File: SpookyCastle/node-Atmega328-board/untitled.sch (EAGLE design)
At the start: 24 parts, among them IC2 MEGA48/88/168-AU, J1 RJ11-6PTH

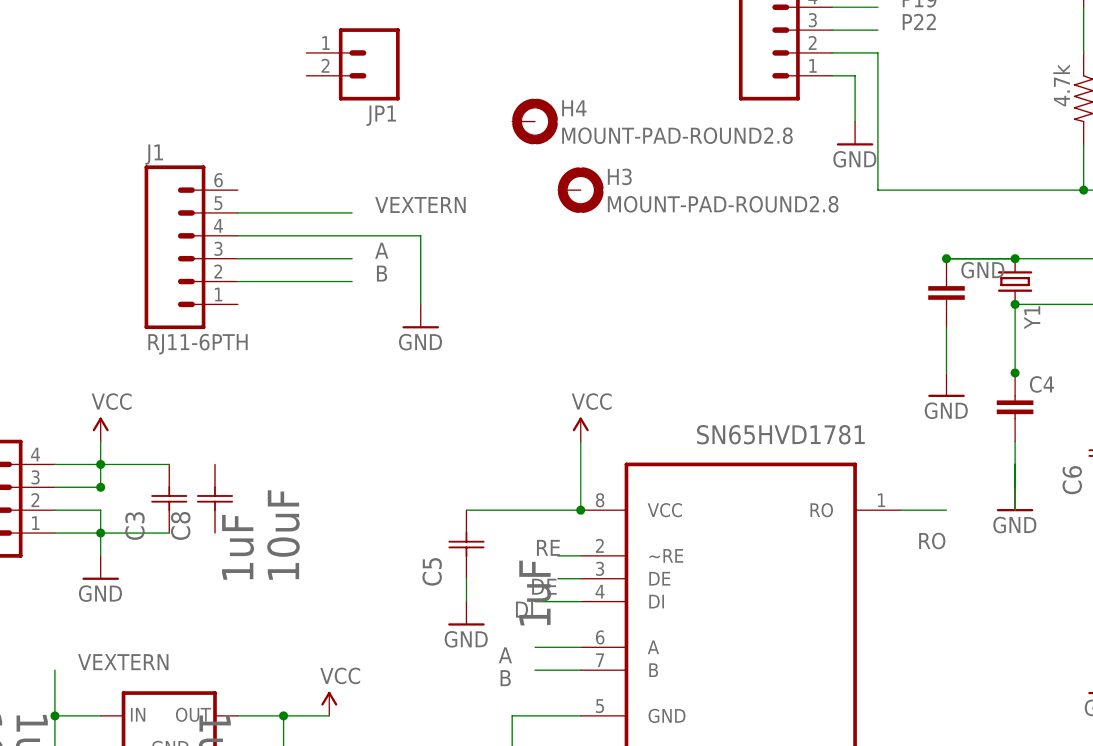
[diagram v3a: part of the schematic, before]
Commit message: Added a buncha silk to the board.
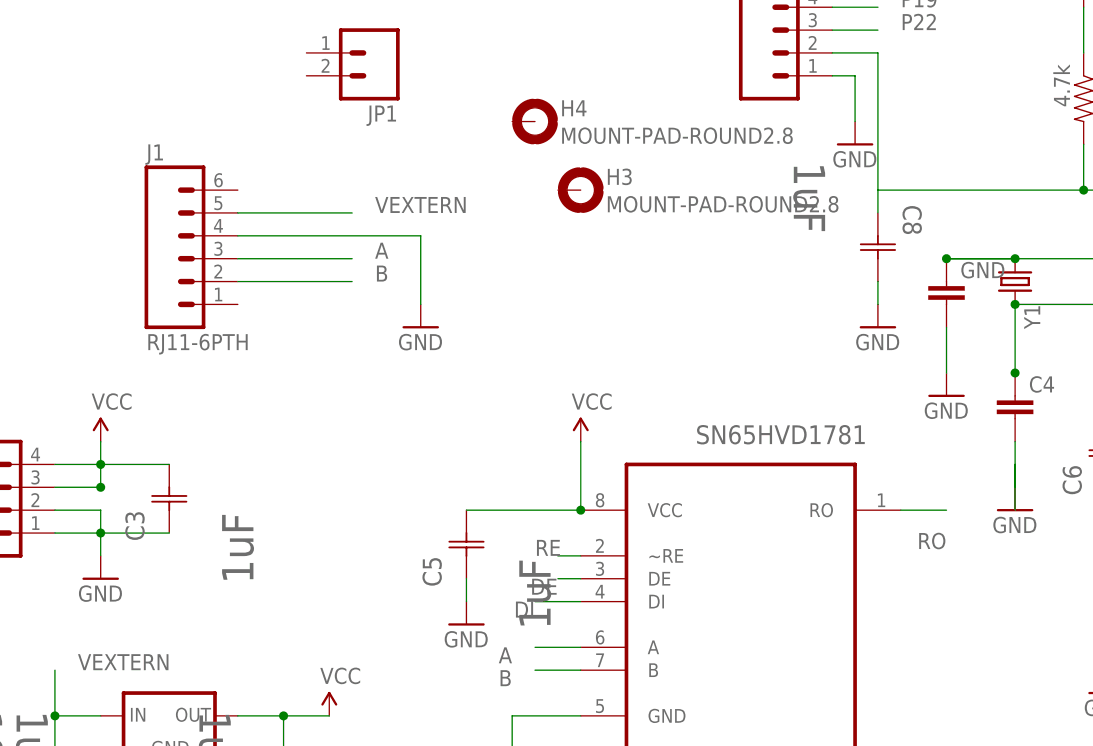
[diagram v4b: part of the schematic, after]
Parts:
- C8: value 10uF -> 1uF; device Murata_By_element14_Batch_1:GRM32ER7YA106KA12L -> Murata_By_element14_Batch_1:GRM21BR71H105KA12L; MPN GRM32ER7YA106KA12L -> GRM21BR71H105KA12L; OC_FARNELL 1735537 -> 1735541; OC_NEWARK 24R2634 -> 24R6342; VALUE 10uF -> 1uF; VOLTAGERATING 35V -> 50V
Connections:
- net GND: now also C8.C2
- net N$22: now also C8.C1
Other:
- moved on the sheet: C8
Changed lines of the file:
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@@
 <part name="R1" library="SparkFun - Copy" deviceset="RESISTOR" device="0805-RES" value="4.7k"/>
 <part name="P+5" library="SparkFun - Copy" deviceset="VCC" device=""/>
-<part name="C8" library="Murata_By_element14_Batch_1" deviceset="GRM32ER7YA106KA12L" device="" value="10uF">
-<attribute name="MPN" value="GRM32ER7YA106KA12L"/>
-<attribute name="OC_FARNELL" value="1735537"/>
-<attribute name="OC_NEWARK" value="24R2634"/>
+<part name="GND11" library="SparkFun - Copy" deviceset="GND" device=""/>
+<part name="C8" library="Murata_By_element14_Batch_1" deviceset="GRM21BR71H105KA12L" device="" value="1uF">
+<attribute name="MPN" value="GRM21BR71H105KA12L "/>
+<attribute name="OC_FARNELL" value="1735541"/>
+<attribute name="OC_NEWARK" value="24R6342"/>
 <attribute name="SUPPLIER" value="Murata"/>
 <attribute name="TOLERANCE" value="±10%"/>
-<attribute name="VALUE" value="10uF"/>
-<attribute name="VOLTAGERATING" value="35V"/>
+<attribute name="VALUE" value="1uF"/>
+<attribute name="VOLTAGERATING" value="50V"/>
 </part>
 </parts>
@@
 <instance part="R1" gate="G$1" x="99.06" y="104.14" rot="R270"/>
 <instance part="P+5" gate="1" x="99.06" y="114.3"/>
-<instance part="C8" gate="A" x="2.54" y="55.88" rot="R90"/>
+<instance part="GND11" gate="1" x="76.2" y="78.74"/>
+<instance part="C8" gate="A" x="76.2" y="91.44" rot="R270"/>
 </instances>
 <busses>
@@
 <wire x1="99.06" y1="99.06" x2="99.06" y2="93.98" width="0.1524" layer="91"/>
 <junction x="99.06" y="93.98"/>
+<pinref part="C8" gate="A" pin="C1"/>
+<wire x1="76.2" y1="91.44" x2="76.2" y2="93.98" width="0.1524" layer="91"/>
 </segment>
 </net>
@@
 <junction x="-15.24" y="22.86"/>
 </segment>
-</net>
+<segment>
+<pinref part="GND11" gate="1" pin="GND"/>
+<pinref part="C8" gate="A" pin="C2"/>
+<wire x1="76.2" y1="81.28" x2="76.2" y2="83.82" width="0.1524" layer="91"/>
+</segment>
+</net>

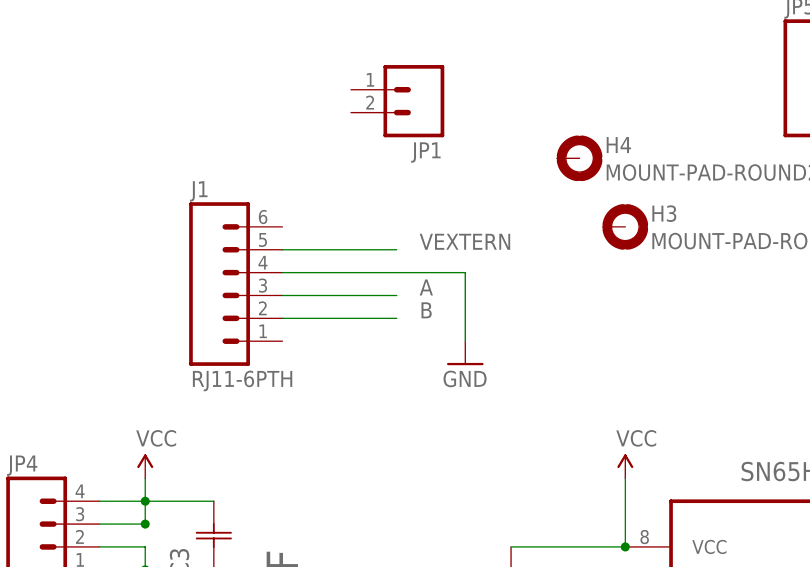
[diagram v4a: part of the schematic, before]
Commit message: Updated board and spec pdf. PDF is all bold due to what I think is an OpenOffice bug.
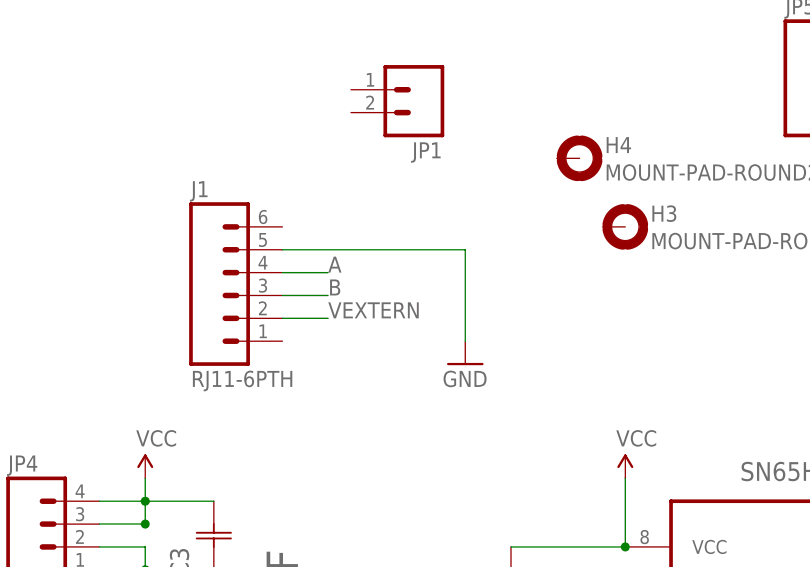
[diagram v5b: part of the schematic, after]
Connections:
- net A: now also J1.4; no longer J1.3
- net B: now also J1.3; no longer J1.2
- net GND: now also J1.5; no longer J1.4
- net VEXTERN: now also J1.2; no longer J1.5
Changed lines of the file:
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@@
 </segment>
 <segment>
-<wire x1="25.4" y1="88.9" x2="25.4" y2="81.28" width="0.1524" layer="91"/>
+<wire x1="25.4" y1="91.44" x2="25.4" y2="81.28" width="0.1524" layer="91"/>
 <pinref part="GND9" gate="1" pin="GND"/>
-<pinref part="J1" gate="G$1" pin="4"/>
-<wire x1="25.4" y1="88.9" x2="5.08" y2="88.9" width="0.1524" layer="91"/>
+<pinref part="J1" gate="G$1" pin="5"/>
+<wire x1="5.08" y1="91.44" x2="25.4" y2="91.44" width="0.1524" layer="91"/>
 </segment>
 <segment>
@@
 </segment>
 <segment>
-<pinref part="J1" gate="G$1" pin="5"/>
-<wire x1="5.08" y1="91.44" x2="17.78" y2="91.44" width="0.1524" layer="91"/>
-<label x="20.32" y="91.44" size="1.778" layer="95"/>
+<pinref part="J1" gate="G$1" pin="2"/>
+<wire x1="5.08" y1="83.82" x2="10.16" y2="83.82" width="0.1524" layer="91"/>
+<label x="10.16" y="83.82" size="1.778" layer="95"/>
 </segment>
 </net>
 <net name="A" class="0">
-<segment>
-<pinref part="J1" gate="G$1" pin="3"/>
-<wire x1="5.08" y1="86.36" x2="17.78" y2="86.36" width="0.1524" layer="91"/>
-<label x="20.32" y="86.36" size="1.778" layer="95"/>
-</segment>
 <segment>
 <pinref part="SN65HVD1781" gate="A" pin="A"/>
@@
 <label x="35.56" y="43.18" size="1.778" layer="95" rot="R180"/>
 </segment>
+<segment>
+<pinref part="J1" gate="G$1" pin="4"/>
+<wire x1="5.08" y1="88.9" x2="10.16" y2="88.9" width="0.1524" layer="91"/>
+<label x="10.16" y="88.9" size="1.778" layer="95"/>
+</segment>
 </net>
 <net name="B" class="0">
-<segment>
-<pinref part="J1" gate="G$1" pin="2"/>
-<wire x1="5.08" y1="83.82" x2="17.78" y2="83.82" width="0.1524" layer="91"/>
-<label x="20.32" y="83.82" size="1.778" layer="95"/>
-</segment>
 <segment>
 <pinref part="SN65HVD1781" gate="A" pin="B"/>
@@
 <label x="35.56" y="40.64" size="1.778" layer="95" rot="R180"/>
 </segment>
+<segment>
+<pinref part="J1" gate="G$1" pin="3"/>
+<wire x1="5.08" y1="86.36" x2="10.16" y2="86.36" width="0.1524" layer="91"/>
+<label x="10.16" y="86.36" size="1.778" layer="95"/>
+</segment>
 </net>

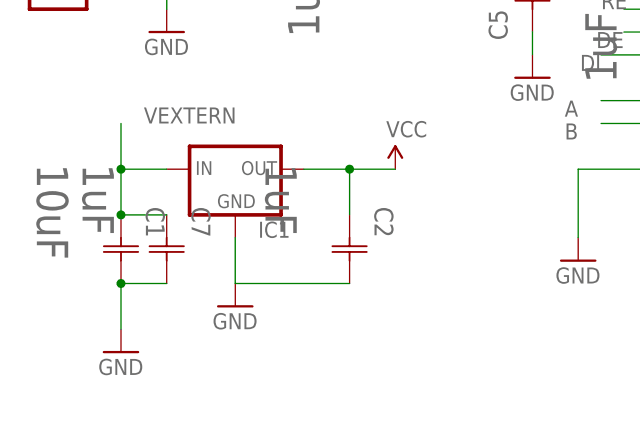
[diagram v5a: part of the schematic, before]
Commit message: Fix critical silk error(Text on wrong side) Add HTML version of the spec since OO is outputting all bold PDFs
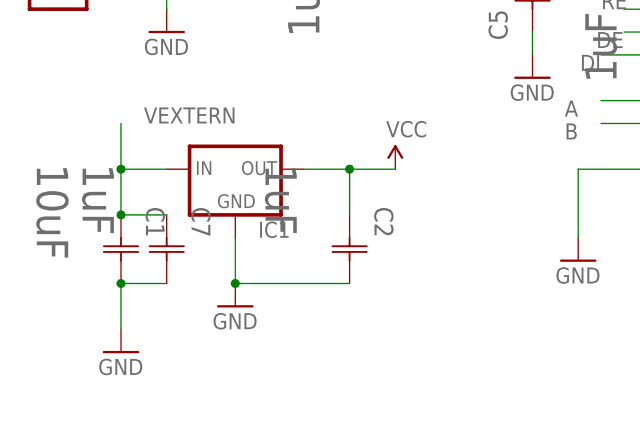
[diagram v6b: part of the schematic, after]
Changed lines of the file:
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@@
 <pinref part="C2" gate="A" pin="C2"/>
 <wire x1="-2.54" y1="22.86" x2="10.16" y2="22.86" width="0.1524" layer="91"/>
+<junction x="-2.54" y="22.86"/>
 </segment>
 <segment>

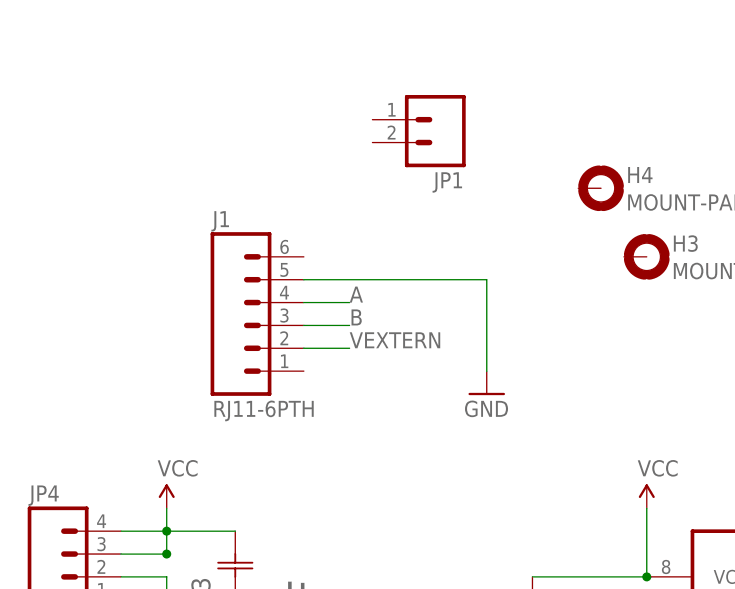
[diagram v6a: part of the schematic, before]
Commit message: Updated the spookycastle board to use screw terminals since the spec no longer requires rj11
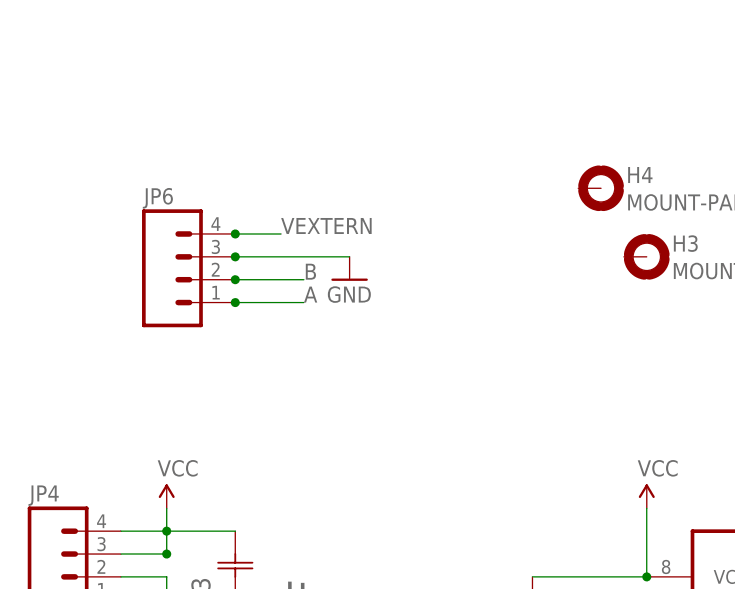
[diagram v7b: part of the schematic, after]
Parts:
- removed J1: RJ11-6PTH, SparkFun - Copy:RJ11-6PTH
- removed JP1: (no value), SparkFun - Copy:M02PTH
- added JP6: (no value), SparkFun - Copy:M04SCREW
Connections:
- net A: now also JP6.1; no longer J1.4
- net B: now also JP6.2; no longer J1.3
- net GND: now also JP6.3; no longer J1.5
- net VEXTERN: now also JP6.4; no longer J1.2
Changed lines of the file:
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@@
 <parts>
 <part name="SN65HVD1781" library="LTC_By_element14_Batch_1" deviceset="LT1785ACS8PBF" device=""/>
-<part name="J1" library="SparkFun - Copy" deviceset="RJ11-6" device="PTH"/>
 <part name="IC1" library="SparkFun - Copy" deviceset="V_REG_78XX" device="SIDE"/>
 <part name="GND1" library="SparkFun - Copy" deviceset="GND" device=""/>
@@
 <part name="GND9" library="SparkFun - Copy" deviceset="GND" device=""/>
 <part name="P+4" library="SparkFun - Copy" deviceset="VCC" device=""/>
-<part name="JP1" library="SparkFun - Copy" deviceset="M02" device="PTH"/>
 <part name="JP5" library="SparkFun - Copy" deviceset="M04" device="LOCK"/>
 <part name="GND10" library="SparkFun - Copy" deviceset="GND" device=""/>
@@
 <attribute name="VOLTAGERATING" value="50V"/>
 </part>
+<part name="JP6" library="SparkFun - Copy" deviceset="M04" device="SCREW"/>
 </parts>
 <sheets>
@@
 <instances>
 <instance part="SN65HVD1781" gate="A" x="60.96" y="50.8"/>
-<instance part="J1" gate="G$1" x="0" y="86.36"/>
 <instance part="IC1" gate="G$1" x="-2.54" y="35.56"/>
 <instance part="GND1" gate="1" x="-15.24" y="15.24"/>
@@
 <instance part="H3" gate="G$1" x="43.18" y="93.98"/>
 <instance part="H4" gate="G$1" x="38.1" y="101.6"/>
-<instance part="GND9" gate="1" x="25.4" y="78.74"/>
+<instance part="GND9" gate="1" x="10.16" y="91.44"/>
 <instance part="P+4" gate="1" x="104.14" y="73.66"/>
-<instance part="JP1" gate="G$1" x="20.32" y="109.22" rot="R180"/>
 <instance part="JP5" gate="G$1" x="66.04" y="109.22"/>
 <instance part="GND10" gate="1" x="73.66" y="99.06"/>
@@
 <instance part="GND11" gate="1" x="76.2" y="78.74"/>
 <instance part="C8" gate="A" x="76.2" y="91.44" rot="R270"/>
+<instance part="JP6" gate="G$1" x="-7.62" y="91.44"/>
 </instances>
 <busses>
@@
 </segment>
 <segment>
-<wire x1="25.4" y1="91.44" x2="25.4" y2="81.28" width="0.1524" layer="91"/>
 <pinref part="GND9" gate="1" pin="GND"/>
-<pinref part="J1" gate="G$1" pin="5"/>
-<wire x1="5.08" y1="91.44" x2="25.4" y2="91.44" width="0.1524" layer="91"/>
+<pinref part="JP6" gate="G$1" pin="3"/>
+<wire x1="-2.54" y1="93.98" x2="10.16" y2="93.98" width="0.1524" layer="91"/>
+<junction x="-2.54" y="93.98"/>
 </segment>
 <segment>
@@
 </segment>
 <segment>
-<pinref part="J1" gate="G$1" pin="2"/>
-<wire x1="5.08" y1="83.82" x2="10.16" y2="83.82" width="0.1524" layer="91"/>
-<label x="10.16" y="83.82" size="1.778" layer="95"/>
+<label x="2.54" y="96.52" size="1.778" layer="95"/>
+<pinref part="JP6" gate="G$1" pin="4"/>
+<wire x1="-2.54" y1="96.52" x2="2.54" y2="96.52" width="0.1524" layer="91"/>
+<junction x="-2.54" y="96.52"/>
 </segment>
 </net>
@@
 </segment>
 <segment>
-<pinref part="J1" gate="G$1" pin="4"/>
-<wire x1="5.08" y1="88.9" x2="10.16" y2="88.9" width="0.1524" layer="91"/>
-<label x="10.16" y="88.9" size="1.778" layer="95"/>
+<label x="5.08" y="88.9" size="1.778" layer="95"/>
+<pinref part="JP6" gate="G$1" pin="1"/>
+<wire x1="-2.54" y1="88.9" x2="5.08" y2="88.9" width="0.1524" layer="91"/>
+<junction x="-2.54" y="88.9"/>
 </segment>
 </net>
@@
 </segment>
 <segment>
-<pinref part="J1" gate="G$1" pin="3"/>
-<wire x1="5.08" y1="86.36" x2="10.16" y2="86.36" width="0.1524" layer="91"/>
-<label x="10.16" y="86.36" size="1.778" layer="95"/>
-</segment>
-</net>
+<label x="5.08" y="91.44" size="1.778" layer="95"/>
+<pinref part="JP6" gate="G$1" pin="2"/>
+<wire x1="-2.54" y1="91.44" x2="5.08" y2="91.44" width="0.1524" layer="91"/>
+<junction x="-2.54" y="91.44"/>
+</segment>
+</net>

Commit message: whole buncha changes
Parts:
- added U$1: OSHW-LOGOM, SparkFun - Copy:OSHW-LOGOM
- C5: value 1uF -> 0.1uF
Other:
- note added: "Can replace with switcher"
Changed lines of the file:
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@@
 <part name="GND3" library="SparkFun - Copy" deviceset="GND" device=""/>
 <part name="GND4" library="SparkFun - Copy" deviceset="GND" device=""/>
-<part name="C5" library="Murata_By_element14_Batch_1" deviceset="GRM21BR71H105KA12L" device="" value="1uF">
+<part name="C5" library="Murata_By_element14_Batch_1" deviceset="GRM21BR71H105KA12L" device="" value="0.1uF">
 <attribute name="MPN" value="GRM21BR71H105KA12L "/>
 <attribute name="OC_FARNELL" value="1735541"/>
@@
 </part>
 <part name="JP6" library="SparkFun - Copy" deviceset="M04" device="SCREW"/>
+<part name="U$1" library="SparkFun - Copy" deviceset="OSHW-LOGO" device="M"/>
 </parts>
 <sheets>
 <sheet>
 <plain>
+<text x="-7.62" y="12.7" size="1.778" layer="97">Can replace with switcher</text>
 </plain>
 <instances>
@@
 <instance part="C8" gate="A" x="76.2" y="91.44" rot="R270"/>
 <instance part="JP6" gate="G$1" x="-7.62" y="91.44"/>
+<instance part="U$1" gate="G$1" x="17.78" y="116.84"/>
 </instances>
 <busses>
@@
 <segment>
 <pinref part="Y1" gate="G$1" pin="1"/>
-<wire x1="83.82" y1="86.36" x2="91.44" y2="86.36" width="0.1524" layer="91"/>
 <pinref part="GND" gate="G$1" pin="1"/>
 <junction x="83.82" y="86.36"/>
@@
 <pinref part="C8" gate="A" pin="C1"/>
 <wire x1="76.2" y1="91.44" x2="76.2" y2="93.98" width="0.1524" layer="91"/>
-</segment>
-</net>
+<junction x="76.2" y="93.98"/>
+</segment>
+</net>
